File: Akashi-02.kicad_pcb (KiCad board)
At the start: 2 copper layers, 52.7 x 80.6 mm, 26 parts, among them CN10 Conn_02x17_Odd_Even, CN7 Conn_02x10_Odd_Even, CN8 Conn_02x08_Odd_Even, CN9 Conn_02x15_Odd_Even, U1 UMB-SSM2603B, U2 UMB-ADAU1361A

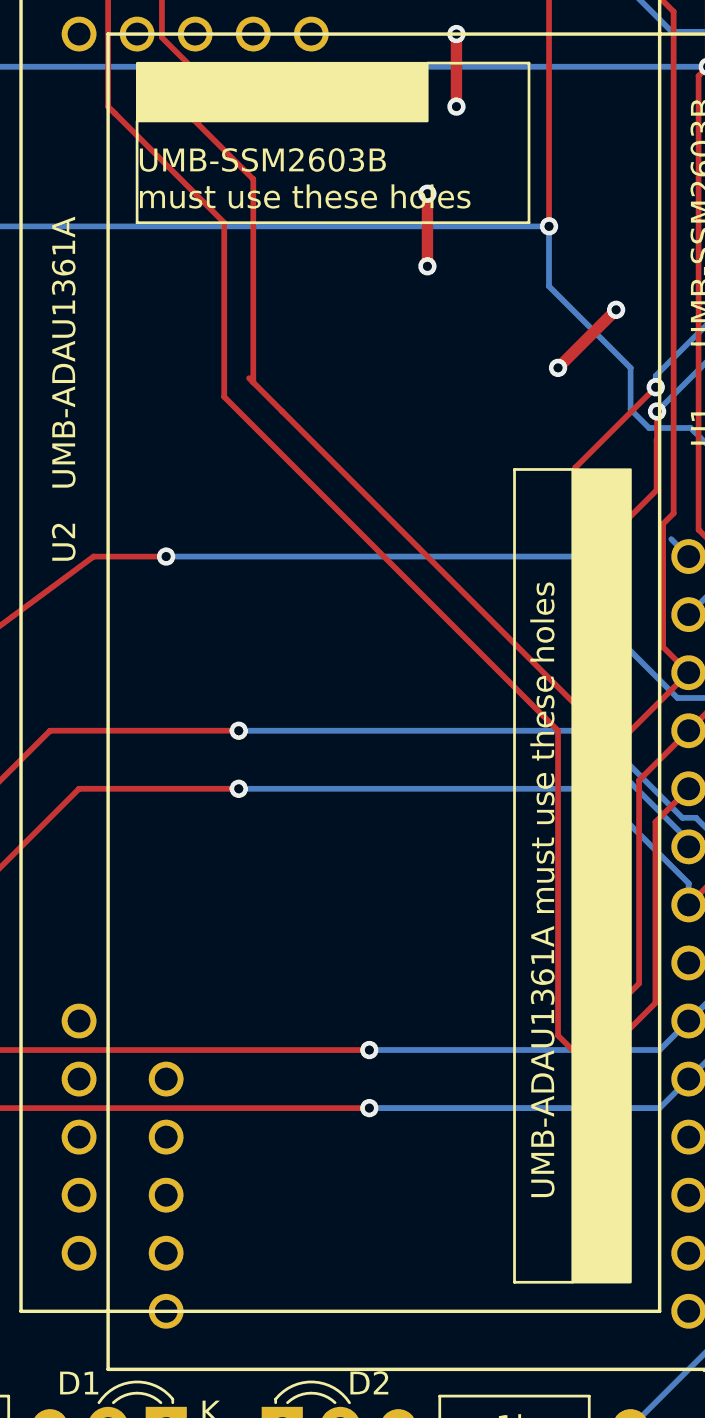
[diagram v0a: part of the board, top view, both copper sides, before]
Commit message: Fix the codec identification
Issue  : CODEC identification is wrong. #4
https://github.com/suikan4github/Akashi-02/issues/4
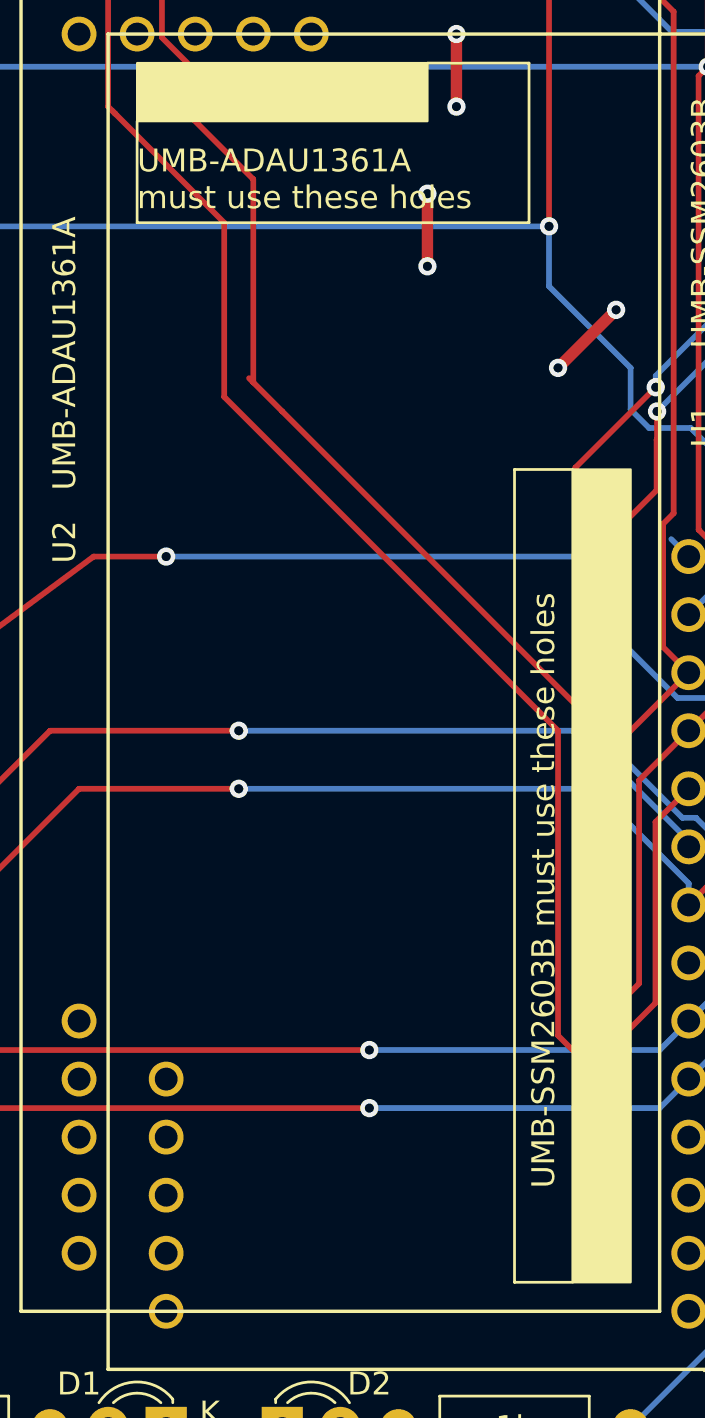
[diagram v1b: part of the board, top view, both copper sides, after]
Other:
- board text added: "Akashi-02 v1.0.2 CODEC Test board for Nucleo 144 (C) Seiichi Horie 2019 https://github.com/suikan4github/Akashi-02"
- board text removed: "Akashi-02 v1.0.1 CODEC Test board for Nucleo 144 (C) Seiichi Horie 2019 https://github.com/suikan4github/Akashi-02"
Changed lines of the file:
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@@
-(kicad_pcb (version 20171130) (host pcbnew 5.1.0-060a0da~80~ubuntu16.04.1)
+(kicad_pcb (version 20171130) (host pcbnew 5.1.2-f72e74a~84~ubuntu16.04.1)
   (general
     (thickness 1.6)
@@
   (gr_line (start 121.92 74.93) (end 121.92 79.375) (layer F.SilkS) (width 0.12))
   (gr_poly (pts (xy 121.92 74.93) (xy 121.92 72.39) (xy 134.62 72.39) (xy 134.62 74.93)) (layer F.SilkS) (width 0.1))
-  (gr_text "UMB-SSM2603B\nmust use these holes" (at 121.92 77.47) (layer F.SilkS)
+  (gr_text "UMB-ADAU1361A\nmust use these holes" (at 121.92 77.47) (layer F.SilkS)
     (effects (font (size 1 1) (thickness 0.15)) (justify left))
   )
-  (gr_text "UMB-ADAU1361A must use these holes" (at 139.7 108.585 90) (layer F.SilkS)
+  (gr_text "UMB-SSM2603B must use these holes" (at 139.7 108.585 90) (layer F.SilkS)
     (effects (font (size 1 1) (thickness 0.15)))
   )
@@
     (effects (font (size 1 1) (thickness 0.15)) (justify left))
   )
-  (gr_text "Akashi-02 v1.0.1\nCODEC Test board for Nucleo 144 \n(C) Seiichi Horie 2019\nhttps://github.com/suikan4github/Akashi-02" (at 130.175 128.27 -90) (layer B.SilkS)
+  (gr_text "Akashi-02 v1.0.2\nCODEC Test board for Nucleo 144 \n(C) Seiichi Horie 2019\nhttps://github.com/suikan4github/Akashi-02" (at 130.175 128.27 -90) (layer B.SilkS)
     (effects (font (size 1.5 1.5) (thickness 0.15)) (justify left mirror))
   )

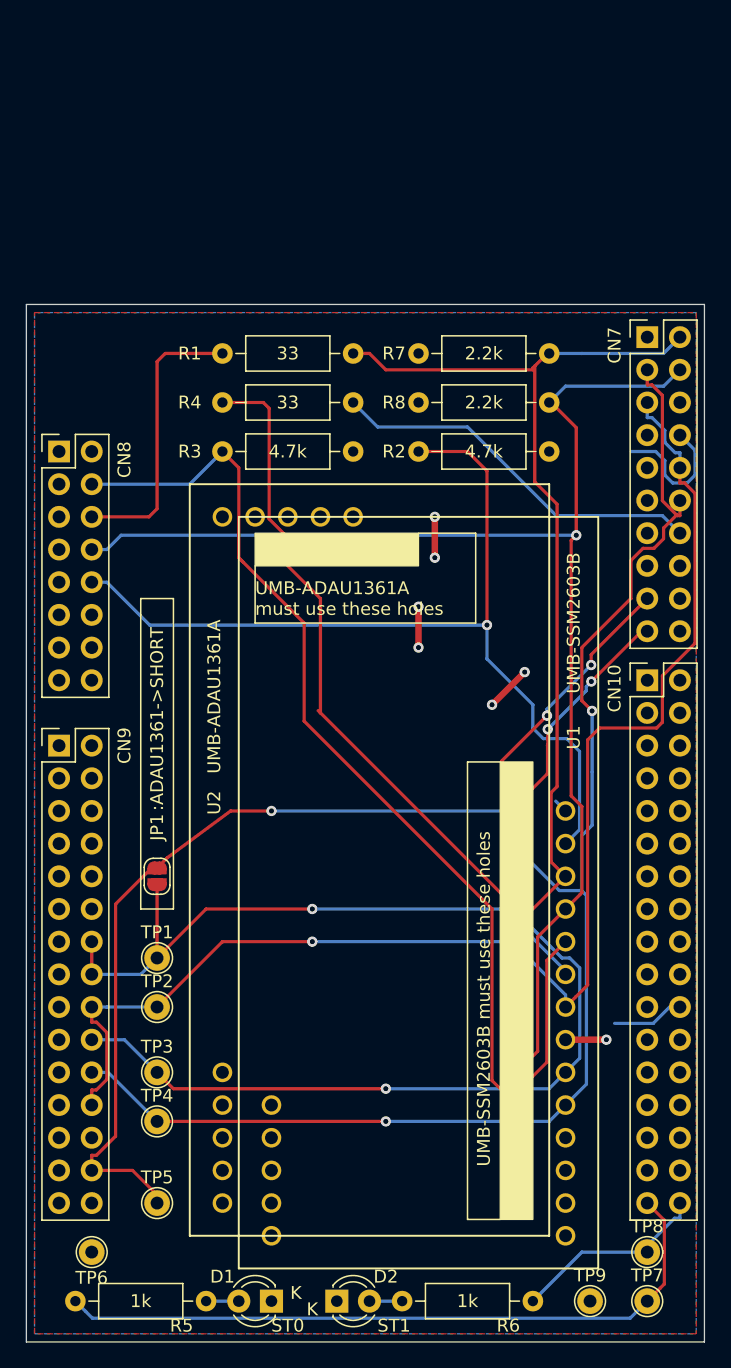
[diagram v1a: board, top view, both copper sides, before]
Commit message: Change the board function and figure.
Issue 5 : U2 Pin4 is set ground by mistake
https://github.com/suikan4github/Akashi-02/issues/5

Issue 6 : Remove SSM2603 support
https://github.com/suikan4github/Akashi-02/issues/6

Issue 7 : Remove SPI support
https://github.com/suikan4github/Akashi-02/issues/7

Issue 8 : Extend the board
https://github.com/suikan4github/Akashi-02/issues/8
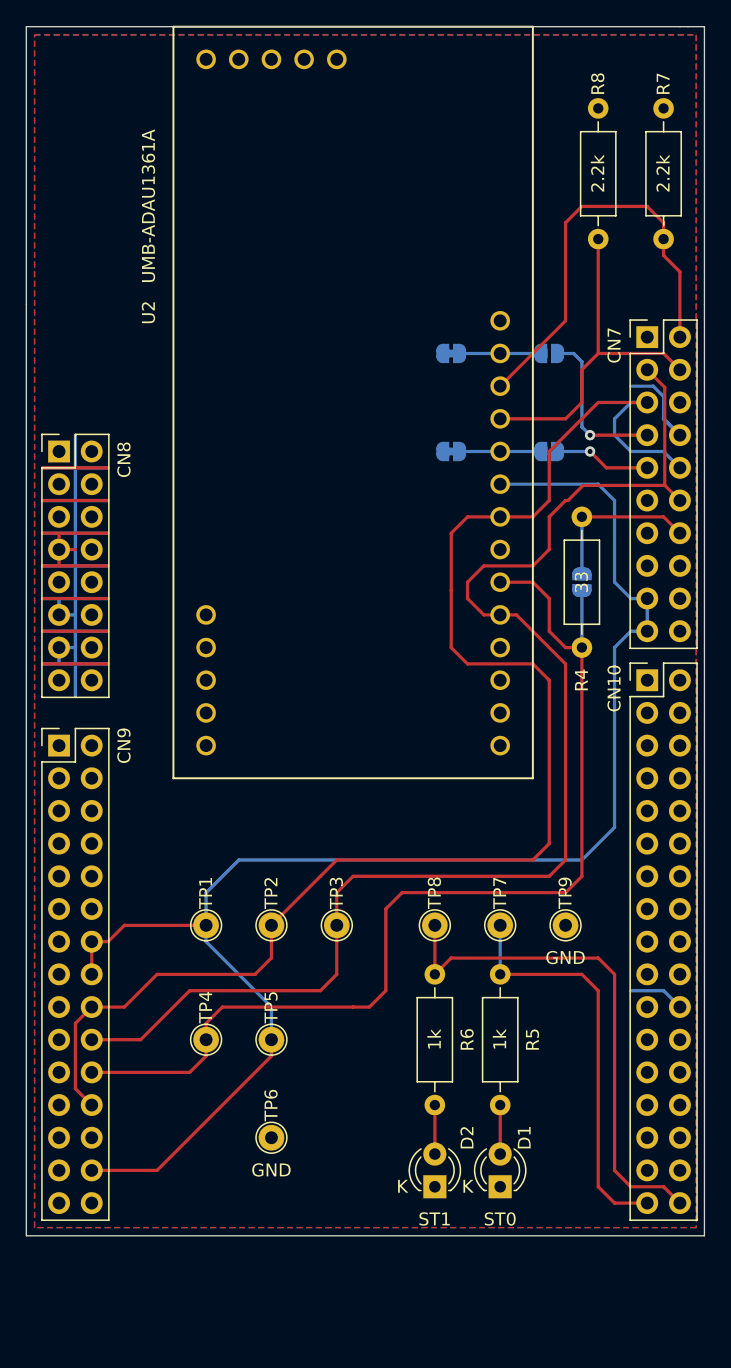
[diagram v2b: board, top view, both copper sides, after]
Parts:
- removed R1: 33, Resistor_THT:R_Axial_DIN0207_L6.3mm_D2.5mm_P10.16mm_Horizontal
- removed R2, R3: 4.7k, Resistor_THT:R_Axial_DIN0207_L6.3mm_D2.5mm_P10.16mm_Horizontal
- removed U1: UMB-SSM2603B, Codec_Modules:UMB-ADAU1361A
- added JP2: SolderJumper_2_Bridged, Jumper:SolderJumper-2_P1.3mm_Bridged_RoundedPad1.0x1.5mm, B.Cu at (137.2, 66.0)
- added JP3: SolderJumper_2_Open, Jumper:SolderJumper-2_P1.3mm_Open_RoundedPad1.0x1.5mm, B.Cu at (144.8, 66.0)
- added JP4: SolderJumper_2_Bridged, Jumper:SolderJumper-2_P1.3mm_Bridged_RoundedPad1.0x1.5mm, B.Cu at (137.2, 58.4)
- added JP5: SolderJumper_2_Open, Jumper:SolderJumper-2_P1.3mm_Open_RoundedPad1.0x1.5mm, B.Cu at (144.8, 58.4)
- JP1: moved to B.Cu
- moved R5 41.7 mm to (141.0, 106.7), turned to 270 degrees
- moved JP1 40.2 mm to (147.3, 76.2), turned to 270 degrees
- moved U2 38.4 mm to (141.0, 88.9)
- moved R4 33.8 mm to (147.3, 81.3), turned to 90 degrees
- moved TP7 31.4 mm to (141.0, 102.9), turned to 180 degrees
- moved TP8 30.3 mm to (135.9, 102.9), turned to 180 degrees
- moved TP9 29.3 mm to (146.1, 102.9)
- moved R7 26.9 mm to (153.7, 39.4), turned to 270 degrees
- moved R8 26.8 mm to (148.6, 39.4), turned to 270 degrees
- moved R6 26.5 mm to (135.9, 106.7), turned to 270 degrees
- moved D1 19.9 mm to (141.0, 123.2), turned to 90 degrees
- moved TP3 18.1 mm to (128.3, 102.9)
- moved TP6 16.6 mm to (123.2, 119.4)
- moved TP5 15.5 mm to (123.2, 111.8)
- moved D2 11.7 mm to (135.9, 123.2), turned to 90 degrees
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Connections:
- CN7 pad 19: /I2S2_WS -> /I2S1_WS
- CN7 pad 7: (no net) -> /ADDR1
- CN7 pad 9: (no net) -> /ADDR0
- CN8 pad 10: /SPI3_MOSI -> (no net)
- CN8 pad 4: /SPI_SS -> (no net)
- CN8 pad 6: /SPI3_SCK -> (no net)
- CN8 pad 8: /I2C1_SDA -> (no net)
- CN9 pad 20: /DAC_SD -> /I2S1_SDI
- CN9 pad 22: /I2S1_SDI -> /DAC_SD
- CN9 pad 28: /I2S2_WS -> /I2S1_WS
- JP1 pad 1: /I2S1_WS -> /I2S1_SD
- JP1 pad 2: /I2S2_WS -> /DAC_SD
- TP3 pad 1: /DAC_SD -> /I2S1_SDI
- TP4 pad 1: /I2S1_SDI -> /DAC_SD
- TP5 pad 1: /I2S2_WS -> /I2S1_WS
- U2 pad 10: /SPI_SS -> Net-(JP2-Pad1)
- U2 pad 13: /SPI3_MOSI -> Net-(JP4-Pad1)
- U2 pad 4: GND -> (no net)
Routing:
- net /SPI_SS: track 85.9 -> 0.00 mm
- net /I2S2_WS: track 80.5 -> 0.00 mm, vias 3 -> 0
- net /I2C1_SDA: track 105.0 -> 27.0 mm, vias 1 -> 0
- net /SPI3_MOSI: track 71.5 -> 0.00 mm, vias 1 -> 0
- net /I2C1_SCL: track 82.4 -> 32.9 mm
- net GND: track 30.3 -> 71.7 mm, vias 7 -> 0
- net +3V3: track 0.00 -> 39.3 mm
- net /I2S1_WS: track 79.5 -> 116.7 mm, vias 3 -> 0
- net /ST1: track 15.8 -> 40.2 mm
- net /DAC_SD: track 105.4 -> 81.8 mm, vias 1 -> 0
- net /ST0: track 54.3 -> 31.5 mm
- net /SPI3_SCK: track 22.1 -> 0.00 mm
- net /I2S1_SD: track 29.6 -> 12.6 mm
- net /ADDR1: track 0.00 -> 12.6 mm, vias 0 -> 1
- net /ADDR0: track 0.00 -> 7.50 mm, vias 0 -> 1
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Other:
- board size 52.7 x 80.6 mm -> 52.7 x 94 mm
- board text added: "Akashi-02 v2.0.0 CODEC board for Nucleo 144 (C) Seiichi Horie 2019 https://github.com/suikan4github/Akashi-02"
- board text added: "GND"
- board text added: "JP1 OPEN SHORT OPEN"
- board text added: "JP5 JP4 JP3 JP2 : I2C ADRS OPEN CLOSE OPEN CLOSE : 0x38 CLOSE OPEN CLOSE OPEN : Prgm Ctrl Prgm Ctrl : I2C Address = 0x38+PB12:PA15"
- board text added: "R4 REMOVE REMOVE INSTALL"
- board text added: "SAI ONLY : I2S ONLY : BOTH :"
- board text removed: ":ADAU1361->SHORT"
- board text removed: "Akashi-02 v1.0.2 CODEC Test board for Nucleo 144 (C) Seiichi Horie 2019 https://github.com/suikan4github/Akashi-02"
- board text removed: "UMB-ADAU1361A must use these holes"
- board text removed: "UMB-SSM2603B must use these holes"

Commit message: Added TOL-POT4 connector. Preparing to release.
- Updated README.md
- Updated pin-config.png
- Updated gerber
- Updated schematics in PDF
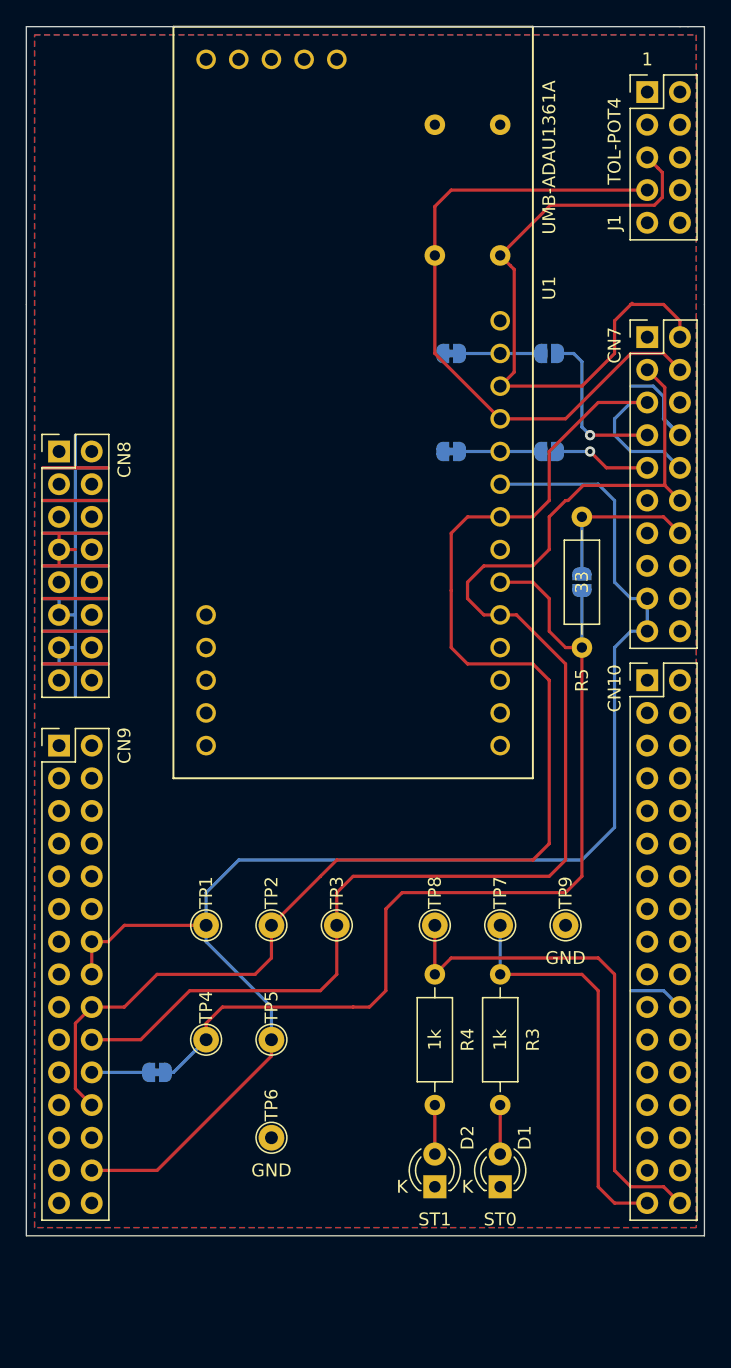
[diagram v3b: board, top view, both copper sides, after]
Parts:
- removed R8: 2.2k, Resistor_THT:R_Axial_DIN0207_L6.3mm_D2.5mm_P10.16mm_Horizontal
- added J1: Conn_02x05_Odd_Even, Connector_PinHeader_2.54mm:PinHeader_2x05_P2.54mm_Vertical, F.Cu at (152.4, 38.1)
- added JP6: SolderJumper_2_Bridged, Jumper:SolderJumper-2_P1.3mm_Bridged_RoundedPad1.0x1.5mm, B.Cu at (114.3, 114.3)
- added R2: 2.2k, Resistor_THT:R_Axial_DIN0207_L6.3mm_D2.5mm_P10.16mm_Horizontal, B.Cu at (135.9, 40.6)
- R1: renamed from R7; moved to B.Cu
- moved R1 12.8 mm to (141.0, 40.6)
- renumbered R5 to R3, R6 to R4, R4 to R5, U2 to U1
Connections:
- CN10 pad 1: (no net) -> Net-(CN10-Pad1)
- CN10 pad 10: (no net) -> Net-(CN10-Pad10)
- CN10 pad 11: (no net) -> Net-(CN10-Pad11)
- CN10 pad 12: (no net) -> Net-(CN10-Pad12)
- CN10 pad 13: (no net) -> Net-(CN10-Pad13)
- CN10 pad 14: (no net) -> Net-(CN10-Pad14)
- CN10 pad 15: (no net) -> Net-(CN10-Pad15)
- CN10 pad 16: (no net) -> Net-(CN10-Pad16)
- CN10 pad 18: (no net) -> Net-(CN10-Pad18)
- CN10 pad 19: (no net) -> Net-(CN10-Pad19)
- CN10 pad 2: (no net) -> Net-(CN10-Pad2)
- CN10 pad 20: (no net) -> Net-(CN10-Pad20)
- CN10 pad 21: (no net) -> Net-(CN10-Pad21)
- CN10 pad 23: (no net) -> Net-(CN10-Pad23)
- CN10 pad 24: (no net) -> Net-(CN10-Pad24)
- CN10 pad 25: (no net) -> Net-(CN10-Pad25)
- CN10 pad 26: (no net) -> Net-(CN10-Pad26)
- CN10 pad 28: (no net) -> Net-(CN10-Pad28)
- CN10 pad 29: (no net) -> Net-(CN10-Pad29)
- CN10 pad 3: (no net) -> Net-(CN10-Pad3)
- CN10 pad 30: (no net) -> Net-(CN10-Pad30)
- CN10 pad 31: (no net) -> Net-(CN10-Pad31)
- CN10 pad 32: (no net) -> Net-(CN10-Pad32)
- CN10 pad 4: (no net) -> Net-(CN10-Pad4)
- CN10 pad 6: (no net) -> Net-(CN10-Pad6)
- CN10 pad 7: (no net) -> Net-(CN10-Pad7)
- CN10 pad 8: (no net) -> Net-(CN10-Pad8)
- CN10 pad 9: (no net) -> Net-(CN10-Pad9)
- CN7 pad 1: (no net) -> Net-(CN7-Pad1)
- CN7 pad 11: (no net) -> Net-(CN7-Pad11)
- CN7 pad 13: (no net) -> Net-(CN7-Pad13)
- CN7 pad 15: (no net) -> Net-(CN7-Pad15)
- CN7 pad 16: (no net) -> Net-(CN7-Pad16)
- CN7 pad 18: (no net) -> Net-(CN7-Pad18)
- CN7 pad 20: (no net) -> Net-(CN7-Pad20)
- CN7 pad 6: (no net) -> Net-(CN7-Pad6)
- CN8 pad 1: (no net) -> Net-(CN8-Pad1)
- CN8 pad 10: (no net) -> Net-(CN8-Pad10)
- CN8 pad 12: (no net) -> Net-(CN8-Pad12)
- CN8 pad 14: (no net) -> Net-(CN8-Pad14)
- CN8 pad 15: (no net) -> Net-(CN8-Pad15)
- CN8 pad 16: (no net) -> Net-(CN8-Pad16)
- CN8 pad 2: (no net) -> Net-(CN8-Pad2)
- CN8 pad 3: (no net) -> Net-(CN8-Pad3)
- CN8 pad 4: (no net) -> Net-(CN8-Pad4)
- CN8 pad 5: (no net) -> Net-(CN8-Pad5)
- CN8 pad 6: (no net) -> Net-(CN8-Pad6)
- CN8 pad 8: (no net) -> Net-(CN8-Pad8)
- CN8 pad 9: (no net) -> Net-(CN8-Pad9)
- CN9 pad 1: (no net) -> Net-(CN9-Pad1)
- CN9 pad 10: (no net) -> Net-(CN9-Pad10)
- CN9 pad 11: (no net) -> Net-(CN9-Pad11)
- CN9 pad 13: (no net) -> Net-(CN9-Pad13)
- CN9 pad 15: (no net) -> Net-(CN9-Pad15)
- CN9 pad 17: (no net) -> Net-(CN9-Pad17)
- CN9 pad 19: (no net) -> Net-(CN9-Pad19)
- CN9 pad 2: (no net) -> Net-(CN9-Pad2)
- CN9 pad 21: (no net) -> Net-(CN9-Pad21)
- CN9 pad 22: /DAC_SD -> /SAI1_SD_B
- CN9 pad 25: (no net) -> Net-(CN9-Pad25)
- CN9 pad 26: (no net) -> Net-(CN9-Pad26)
- CN9 pad 27: (no net) -> Net-(CN9-Pad27)
- CN9 pad 29: (no net) -> Net-(CN9-Pad29)
- CN9 pad 3: (no net) -> Net-(CN9-Pad3)
- CN9 pad 30: (no net) -> Net-(CN9-Pad30)
- CN9 pad 4: (no net) -> Net-(CN9-Pad4)
- CN9 pad 5: (no net) -> Net-(CN9-Pad5)
- CN9 pad 6: (no net) -> Net-(CN9-Pad6)
- CN9 pad 7: (no net) -> Net-(CN9-Pad7)
- CN9 pad 8: (no net) -> Net-(CN9-Pad8)
- CN9 pad 9: (no net) -> Net-(CN9-Pad9)
- U1 pad 15: (no net) -> Net-(U1-Pad15)
- U1 pad 16: (no net) -> Net-(U1-Pad16)
- U1 pad 17: (no net) -> Net-(U1-Pad17)
- U1 pad 18: (no net) -> Net-(U1-Pad18)
- U1 pad 19: (no net) -> Net-(U1-Pad19)
- U1 pad 20: (no net) -> Net-(U1-Pad20)
- U1 pad 21: (no net) -> Net-(U1-Pad21)
- U1 pad 22: (no net) -> Net-(U1-Pad22)
- U1 pad 23: (no net) -> Net-(U1-Pad23)
- U1 pad 24: (no net) -> Net-(U1-Pad24)
- U1 pad 3: (no net) -> Net-(U1-Pad3)
- U1 pad 4: (no net) -> Net-(U1-Pad4)
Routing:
- net /I2C1_SDA: track 27.0 -> 52.3 mm
- net /I2C1_SCL: track 32.9 -> 49.1 mm
- net /DAC_SD: track 81.8 -> 75.3 mm
- net /SAI1_SD_B: track 0.00 -> 4.43 mm
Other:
- board text added: "1"
- board text added: "JP5 JP4 JP3 JP2 : I2C ADRS OPENED CLOSED OPENED CLOSED : 0x38 CLOSED OPENED CLOSED OPENED : Prg Ctrl Prg Ctrl : I2C Address = 0x38+PB12:PA15"
- board text added: "SAI : R5=Removed, JP1=Opened, JP6=Closed I2S : R5=Removed, JP1=Closed, JP6=Opened BOTH : R5=Install, JP1=Opened, JP6=Closed"
- board text added: "TOL-POT4"
- board text removed: "JP1 OPEN SHORT OPEN"
- board text removed: "JP5 JP4 JP3 JP2 : I2C ADRS OPEN CLOSE OPEN CLOSE : 0x38 CLOSE OPEN CLOSE OPEN : Prgm Ctrl Prgm Ctrl : I2C Address = 0x38+PB12:PA15"
- board text removed: "R4 REMOVE REMOVE INSTALL"
- board text removed: "SAI ONLY : I2S ONLY : BOTH :"
